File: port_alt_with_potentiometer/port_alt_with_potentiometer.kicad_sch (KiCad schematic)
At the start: 5 parts, among them U2 2652, U3 NODEMCU32S

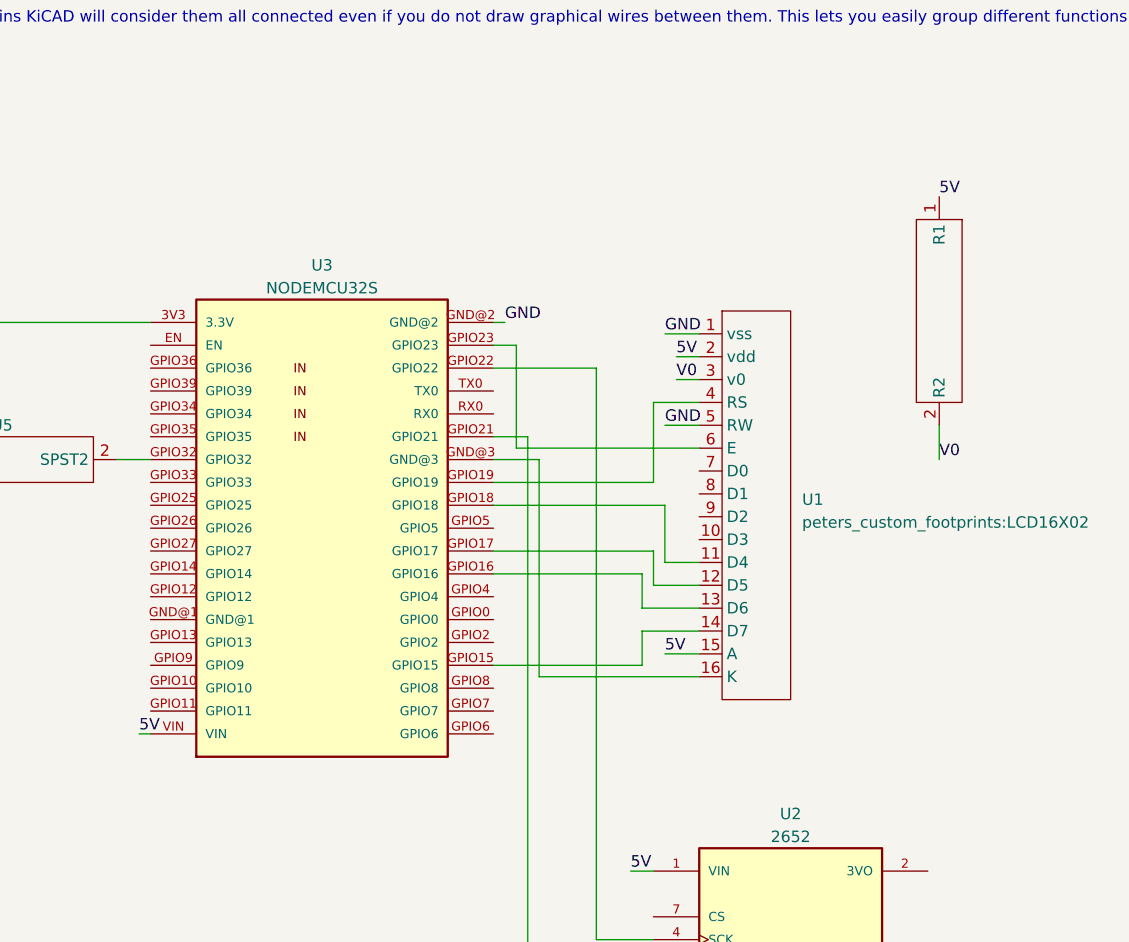
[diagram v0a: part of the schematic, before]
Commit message: incorporated rate functions
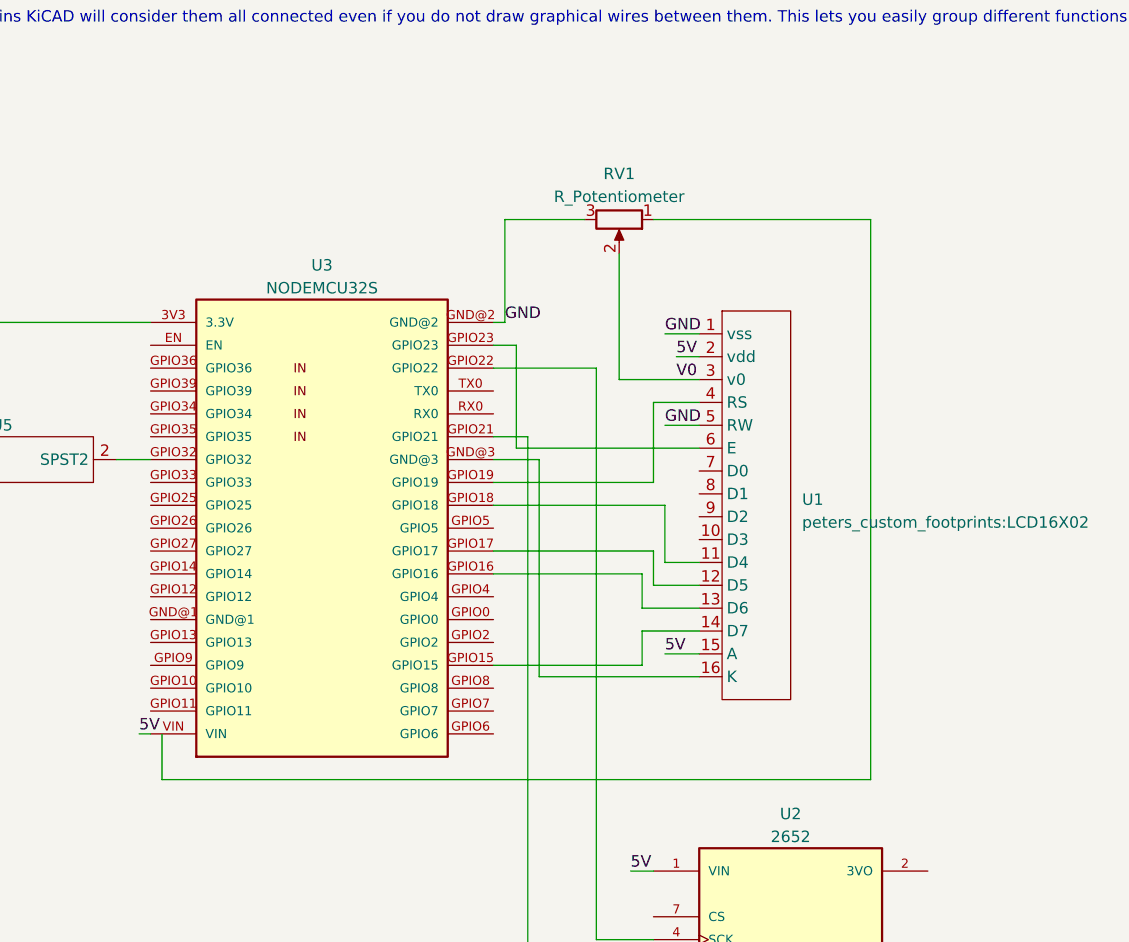
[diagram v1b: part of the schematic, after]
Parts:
- removed U6: ~, Resistor_THT:R_Axial_DIN0207_L6.3mm_D2.5mm_P10.16mm_Horizontal, symbol New_Library:pushbutton_1
- added RV1: R_Potentiometer, symbol Device:R_Potentiometer
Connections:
- net GND: now also RV1.3
- net V0: now also RV1.2
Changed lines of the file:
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@@
+    (stroke (width 0) (type default))
+  )
+  (wire (pts (xy 187.96 41.91) (xy 187.96 104.14))
     (stroke (width 0) (type default))
   )
@@
     (stroke (width 0) (type default))
   )
+  (wire (pts (xy 187.96 104.14) (xy 109.22 104.14))
+    (stroke (width 0) (type default))
+  )
+  (wire (pts (xy 109.22 99.06) (xy 109.22 104.14))
+    (stroke (width 0) (type default))
+  )
   (wire (pts (xy 151.13 92.71) (xy 151.13 68.58))
     (stroke (width 0) (type default))
   )
+  (wire (pts (xy 160.02 45.72) (xy 160.02 59.69))
+    (stroke (width 0) (type default))
+  )
   (wire (pts (xy 168.91 87.63) (xy 162.56 87.63))
     (stroke (width 0) (type default))
@@
     (stroke (width 0) (type default))
   )
-  (wire (pts (xy 195.58 68.58) (xy 195.58 64.77))
+  (wire (pts (xy 156.21 41.91) (xy 147.32 41.91))
     (stroke (width 0) (type default))
   )
@@
     (stroke (width 0) (type default))
   )
+  (wire (pts (xy 147.32 41.91) (xy 147.32 53.34))
+    (stroke (width 0) (type default))
+  )
+  (wire (pts (xy 163.83 41.91) (xy 187.96 41.91))
+    (stroke (width 0) (type default))
+  )
   (wire (pts (xy 196.85 129.54) (xy 194.31 129.54))
     (stroke (width 0) (type default))
@@
     (stroke (width 0) (type default))
   )
-  (wire (pts (xy 166.37 59.69) (xy 168.91 59.69))
+  (wire (pts (xy 160.02 59.69) (xy 168.91 59.69))
     (stroke (width 0) (type default))
   )
@@
     (effects (font (size 1.27 1.27)) (justify left bottom))
   )
-  (label "V0" (at 195.58 68.58 0) (fields_autoplaced)
-    (effects (font (size 1.27 1.27)) (justify left bottom))
-  )
   (label "V0" (at 166.37 59.69 0) (fields_autoplaced)
     (effects (font (size 1.27 1.27)) (justify left bottom))
@@
     (effects (font (size 1.27 1.27)) (justify left bottom))
   )
-  (label "5V" (at 195.58 39.37 0) (fields_autoplaced)
-    (effects (font (size 1.27 1.27)) (justify left bottom))
-  )
   (label "GND" (at 147.32 53.34 0) (fields_autoplaced)
     (effects (font (size 1.27 1.27)) (justify left bottom))
@@
     (effects (font (size 1.27 1.27)) (justify left bottom))
   )
-  (symbol (lib_id "New_Library:pushbutton_1") (at 114.3 83.82 0) (unit 1)
-    (in_bom yes) (on_board yes) (dnp no) (fields_autoplaced)
-    (property "Reference" "U5" (at 91.44 64.77 0)
-      (effects (font (size 1.27 1.27)))
-    )
-    (property "Value" "~" (at 114.3 83.82 0)
-      (effects (font (size 1.27 1.27)))
-    )
-    (property "Footprint" "Resistor_THT:R_Axial_DIN0207_L6.3mm_D2.5mm_P10.16mm_Horizontal" (at 114.3 83.82 0)
-      (effects (font (size 1.27 1.27)) hide)
-    )
-    (property "Datasheet" "" (at 114.3 83.82 0)
+  (symbol (lib_id "Device:R_Potentiometer") (at 160.02 41.91 270) (unit 1)
+    (in_bom yes) (on_board yes) (dnp no) (fields_autoplaced)
+    (property "Reference" "RV1" (at 160.02 36.83 90)
+      (effects (font (size 1.27 1.27)))
+    )
+    (property "Value" "R_Potentiometer" (at 160.02 39.37 90)
+      (effects (font (size 1.27 1.27)))
+    )
+    (property "Footprint" "" (at 160.02 41.91 0)
+      (effects (font (size 1.27 1.27)) hide)
+    )
+    (property "Datasheet" "~" (at 160.02 41.91 0)
       (effects (font (size 1.27 1.27)) hide)
     )
     (pin "1")
     (pin "2")
-    (instances
-      (project "port_alt"
+    (pin "3")
+    (instances
+      (project "port_alt_with_potentiometer"
+        (path "/baa04b76-6fb6-47fa-abc3-aa91b475b2fa"
+          (reference "RV1") (unit 1)
+        )
+      )
+    )
+  )
+  (symbol (lib_id "New_Library:pushbutton_1") (at 114.3 83.82 0) (unit 1)
+    (in_bom yes) (on_board yes) (dnp no) (fields_autoplaced)
+    (property "Reference" "U5" (at 91.44 64.77 0)
+      (effects (font (size 1.27 1.27)))
+    )
+    (property "Value" "~" (at 114.3 83.82 0)
+      (effects (font (size 1.27 1.27)))
+    )
+    (property "Footprint" "Resistor_THT:R_Axial_DIN0207_L6.3mm_D2.5mm_P10.16mm_Horizontal" (at 114.3 83.82 0)
+      (effects (font (size 1.27 1.27)) hide)
+    )
+    (property "Datasheet" "" (at 114.3 83.82 0)
+      (effects (font (size 1.27 1.27)) hide)
+    )
+    (pin "1")
+    (pin "2")
+    (instances
+      (project "port_alt_with_potentiometer"
         (path "/baa04b76-6fb6-47fa-abc3-aa91b475b2fa"
           (reference "U5") (unit 1)
@@
     (pin "7")
     (instances
-      (project "port_alt"
+      (project "port_alt_with_potentiometer"
         (path "/baa04b76-6fb6-47fa-abc3-aa91b475b2fa"
           (reference "U2") (unit 1)
@@
     (pin "9")
     (instances
-      (project "port_alt"
+      (project "port_alt_with_potentiometer"
         (path "/baa04b76-6fb6-47fa-abc3-aa91b475b2fa"
           (reference "U1") (unit 1)
-        )
-      )
-    )
-  )
-  (symbol (lib_name "pushbutton_1_1") (lib_id "New_Library:pushbutton_1") (at 180.34 74.93 270) (unit 1)
-    (in_bom yes) (on_board yes) (dnp no) (fields_autoplaced)
-    (property "Reference" "U6" (at 202.565 93.98 90)
-      (effects (font (size 1.27 1.27)) (justify left) hide)
-    )
-    (property "Value" "~" (at 180.34 74.93 0)
-      (effects (font (size 1.27 1.27)))
-    )
-    (property "Footprint" "Resistor_THT:R_Axial_DIN0207_L6.3mm_D2.5mm_P10.16mm_Horizontal" (at 180.34 74.93 0)
-      (effects (font (size 1.27 1.27)) hide)
-    )
-    (property "Datasheet" "" (at 180.34 74.93 0)
-      (effects (font (size 1.27 1.27)) hide)
-    )
-    (pin "1")
-    (pin "2")
-    (instances
-      (project "port_alt"
-        (path "/baa04b76-6fb6-47fa-abc3-aa91b475b2fa"
-          (reference "U6") (unit 1)
         )
       )
@@
     (pin "VIN")
     (instances
-      (project "port_alt"
+      (project "port_alt_with_potentiometer"
         (path "/baa04b76-6fb6-47fa-abc3-aa91b475b2fa"
           (reference "U3") (unit 1)
